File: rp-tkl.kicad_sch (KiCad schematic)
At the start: 33 parts, among them J1 USB_C_Receptacle_USB2.0, J2 SWD, SW0 SW_Push, U1 XC6206PxxxMR, U2 RP2040, U3 SRV05-4, U4 W25Q128JVS, Y1 12MHz

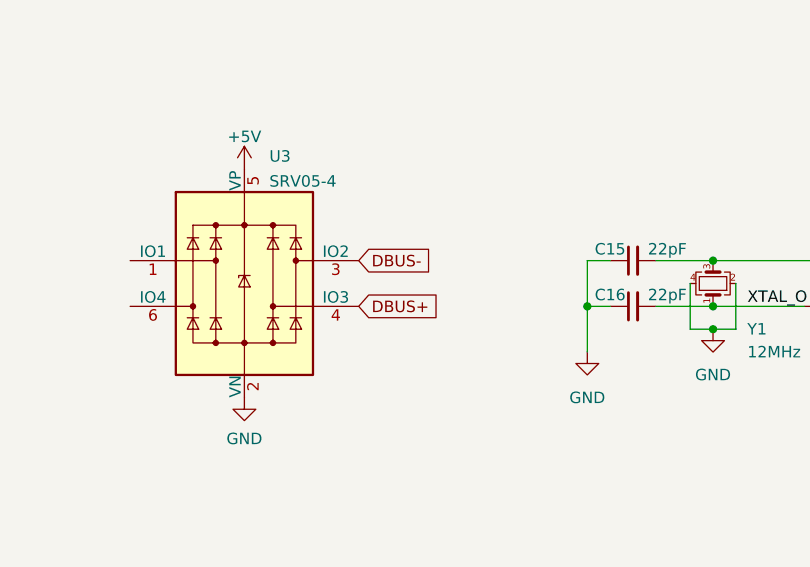
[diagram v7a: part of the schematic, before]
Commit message: Further work on routing
Added GND fills, wired USB more

Need to do:
MCU area
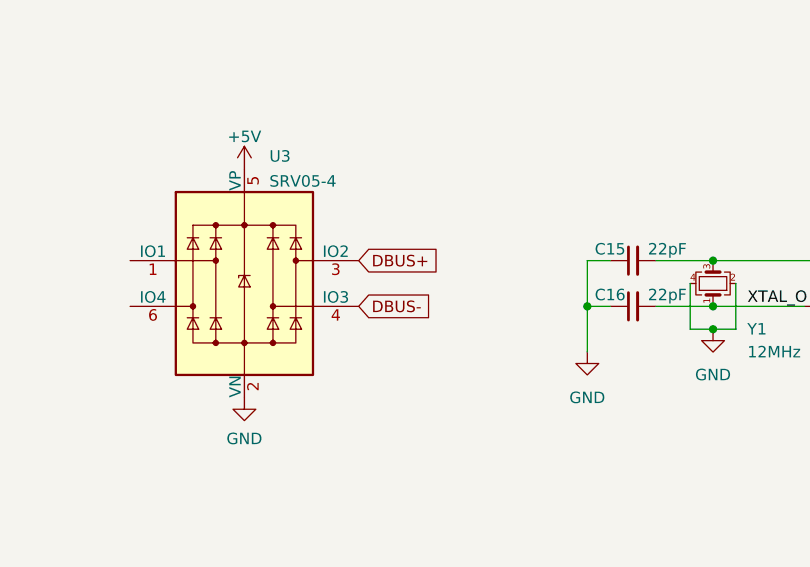
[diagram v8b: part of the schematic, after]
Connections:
- net DBUS+: now also U3.3 (IO2); no longer U3.4 (IO3)
- net DBUS-: now also U3.4 (IO3); no longer U3.3 (IO2)
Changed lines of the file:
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@@
     (effects (font (size 1.27 1.27)) (justify left bottom))
   )
-  (global_label "DBUS+" (shape input) (at 143.51 118.11 0) (fields_autoplaced)
+  (global_label "DBUS+" (shape input) (at 143.51 113.03 0) (fields_autoplaced)
     (effects (font (size 1.27 1.27)) (justify left))
-    (property "Intersheet References" "${INTERSHEET_REFS}" (id 0) (at 152.5755 118.0306 0)
+    (property "Intersheet References" "${INTERSHEET_REFS}" (id 0) (at 152.5755 112.9506 0)
       (effects (font (size 1.27 1.27)) (justify left) hide)
     )
@@
     )
   )
-  (global_label "DBUS-" (shape input) (at 143.51 113.03 0) (fields_autoplaced)
+  (global_label "DBUS-" (shape input) (at 143.51 118.11 0) (fields_autoplaced)
     (effects (font (size 1.27 1.27)) (justify left))
-    (property "Intersheet References" "${INTERSHEET_REFS}" (id 0) (at 152.5755 112.9506 0)
+    (property "Intersheet References" "${INTERSHEET_REFS}" (id 0) (at 152.5755 118.0306 0)
       (effects (font (size 1.27 1.27)) (justify left) hide)
     )
